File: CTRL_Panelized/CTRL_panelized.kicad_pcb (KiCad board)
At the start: 2 copper layers, 72.8 x 111.2 mm, 101 parts, among them J1 503480-0540, J1 5034801400, J2 503480-0440, J2 503480-0800, J2 AYF530365TA, J3 5034801400, J4 503480-0440, J5 503480-0540, U1 74LVC1G08, U1 DRV5033FAxDBZ, U2 74LVC1G08, U2 DRV5033FAxDBZ

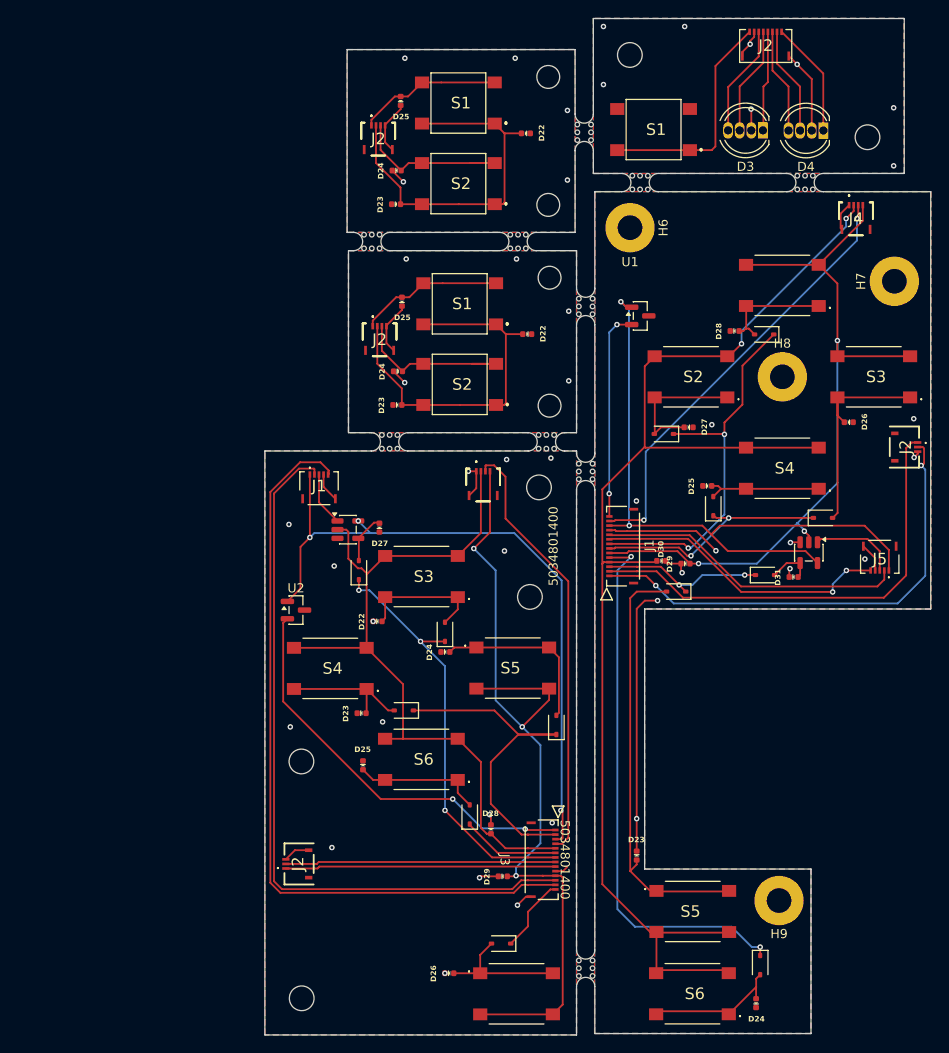
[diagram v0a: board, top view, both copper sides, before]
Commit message: Routed 1V8, 3V3 and 9V voltage regulators
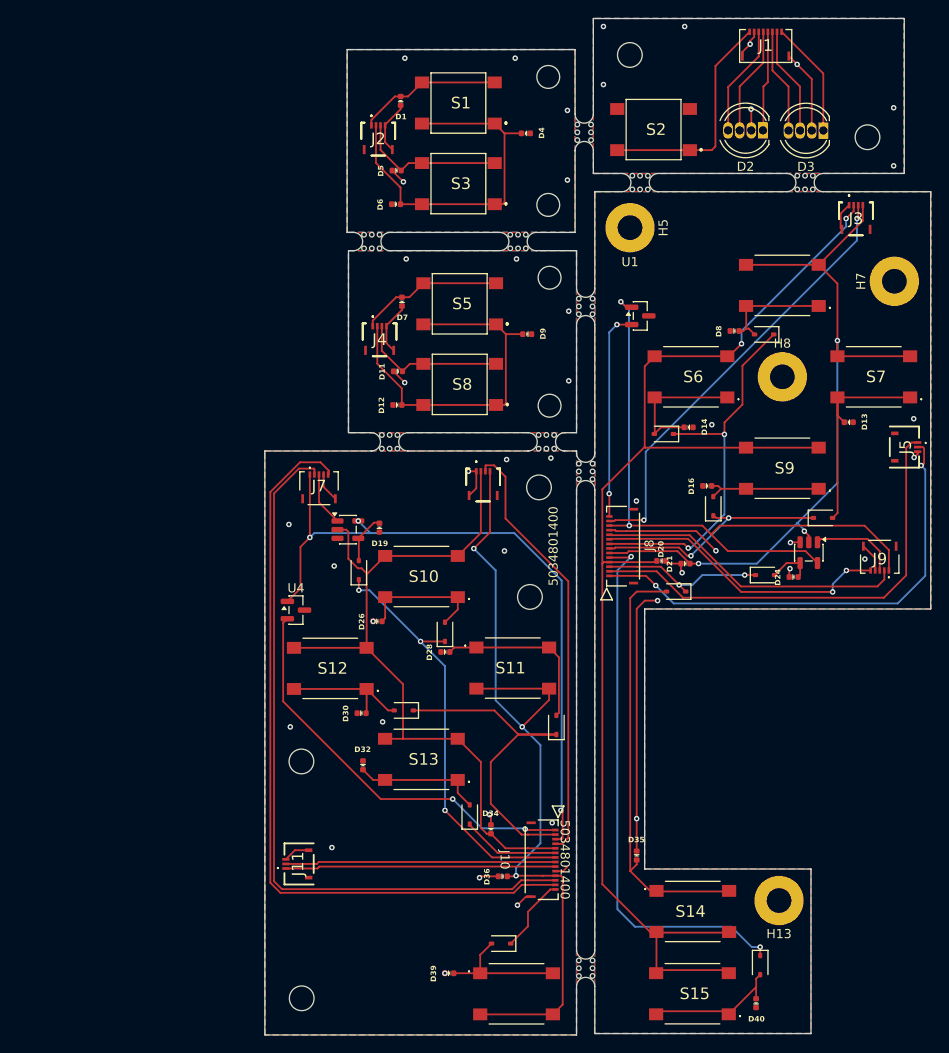
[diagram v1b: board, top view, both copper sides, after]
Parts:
- renumbered D25 to D1, D1 to D10, D24 to D11, D23 to D12, D26 to D13, D27 to D14, D2 to D15, D25 to D16, D4 to D17, D3 to D18, D27 to D19, D3 to D2, D30 to D20, D29 to D21, D8 to D22, D7 to D23, D31 to D24, D5 to D25, D22 to D26, D3 to D27, D24 to D28, D4 to D29, D4 to D3, D23 to D30, D5 to D31, D25 to D32, D6 to D33, D28 to D34, D23 to D35, D29 to D36, D7 to D37, D6 to D38, D26 to D39, D22 to D4, D24 to D40, D24 to D5, D23 to D6, D25 to D7, D28 to D8, D22 to D9, H1 to H10, H2 to H11, H3 to H12, H9 to H13, H4 to H14, H3 to H2, H2 to H3, H2 to H4, H6 to H5, H3 to H6, H2 to H9, J2 to J1, J3 to J10, J2 to J11, J4 to J3, J2 to J4, J2 to J5, J4 to J6, J1 to J7, J1 to J8, J5 to J9, S3 to S10, S5 to S11, S4 to S12, S6 to S13, S5 to S14, S6 to S15, S7 to S16, S1 to S2, S2 to S3, S1 to S4, S1 to S5, S2 to S6, S3 to S7, S2 to S8, S4 to S9, U1 to U2, U2 to U3, U2 to U4, kibuzzard-6A70E37C to kibuzzard-1, kibuzzard-6A70E37C to kibuzzard-2, kibuzzard-6A187131 to kibuzzard-3, kibuzzard-6A186FEC to kibuzzard-4, kibuzzard-6A19F3B7 to kibuzzard-5, kibuzzard-6A187131 to kibuzzard-6
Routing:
- net ColA: track 38.2 -> 32.9 mm
- net +3V3: track 149.7 -> 149.2 mm

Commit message: Some fixes and stuff. i guess.
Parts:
- removed the REF** at (120.7, 54.1)
- removed the REF** at (103.5, 54.1)
- added REF**: MouseBite-Slot_2.0x2.0mm_outset_D0.5mm_P0.85mm_3h, Panelization:MouseBite-Slot_2.0x2.0mm_outset_D0.5mm_P0.85mm_3h, F.Cu at (124.0, 40.2)
- moved D9 75.0 mm to (82.5, 109.0)
- moved J4 75.0 mm to (66.4, 109.7)
- moved D11 75.0 mm to (68.4, 113.1)
- moved D12 75.0 mm to (68.3, 116.8)
- moved D7 75.0 mm to (68.8, 105.5)
- moved H6 75.0 mm to (84.9, 102.9)
- moved H9 75.0 mm to (84.9, 116.9)
- moved REF** 75.0 mm to (89.9, 106.0)
- moved S5 75.0 mm to (75.1, 105.7)
- moved S8 75.0 mm to (75.1, 114.5)
- moved kibuzzard-2 75.0 mm to (72.7, 117.9)
- moved D1 74.9 mm to (68.8, 83.5)
- moved D4 74.9 mm to (82.5, 87.1)
- moved D5 74.9 mm to (68.4, 91.1)
- moved D6 74.9 mm to (68.3, 94.8)
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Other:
- board size 72.8 x 111.2 mm -> 99.8 x 92.2 mm

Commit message: Fixed 3DS Volume slider connector (3 -> 4pin)*
*Changed only in CTRL_Panelized. Seperated PCBs will be updated once all changes are done.
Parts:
- J11, J5: value AYF530365TA -> 503480-0440; footprint AYF530365TA:AYF530365T -> 503480-0440:5034800440
- moved J11 0.25 mm to (93.6, 101.5)
- moved J5 0.24 mm to (159.8, 55.4)
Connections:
- J11 pad 1: SL_VIN -> GND
- J11 pad 2: SL_VOL -> SL_VIN
- J11 pad 3: GND -> SL_VOL
- J5 pad 1: SL_VIN -> GND
- J5 pad 2: SL_BRI -> SL_VIN
- J5 pad 3: GND -> SL_BRI

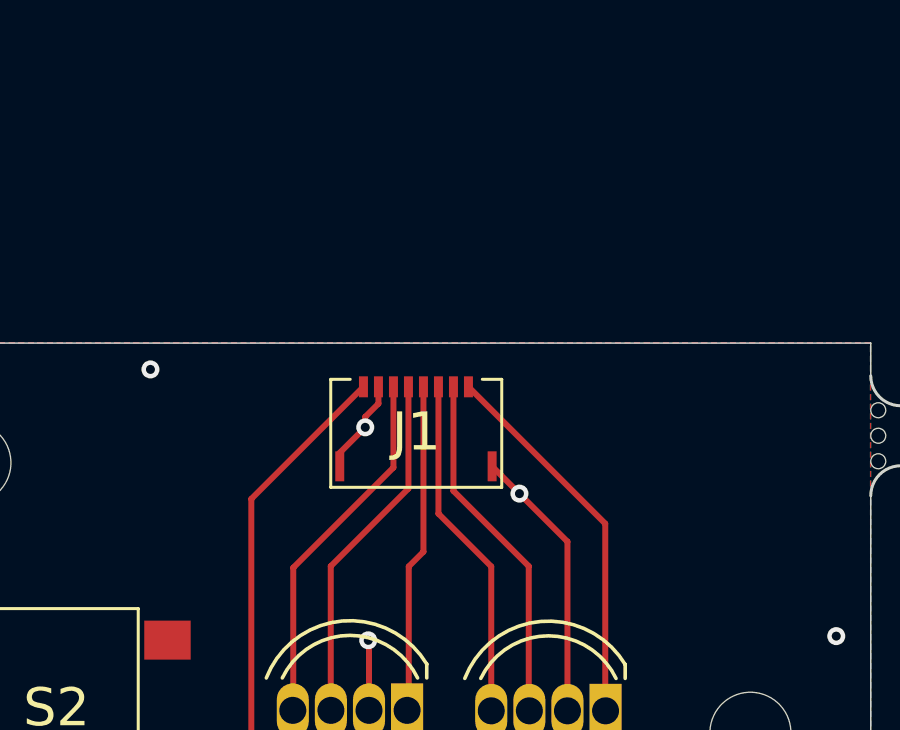
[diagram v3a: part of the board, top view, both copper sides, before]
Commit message: Majorly reworked Display system, condensed and fixed BOM, and many other schematic and design cleanups. \Programs folder was also cleaned up.
Everything is still a work in progress, many things are now unfinished, especially the PCB.
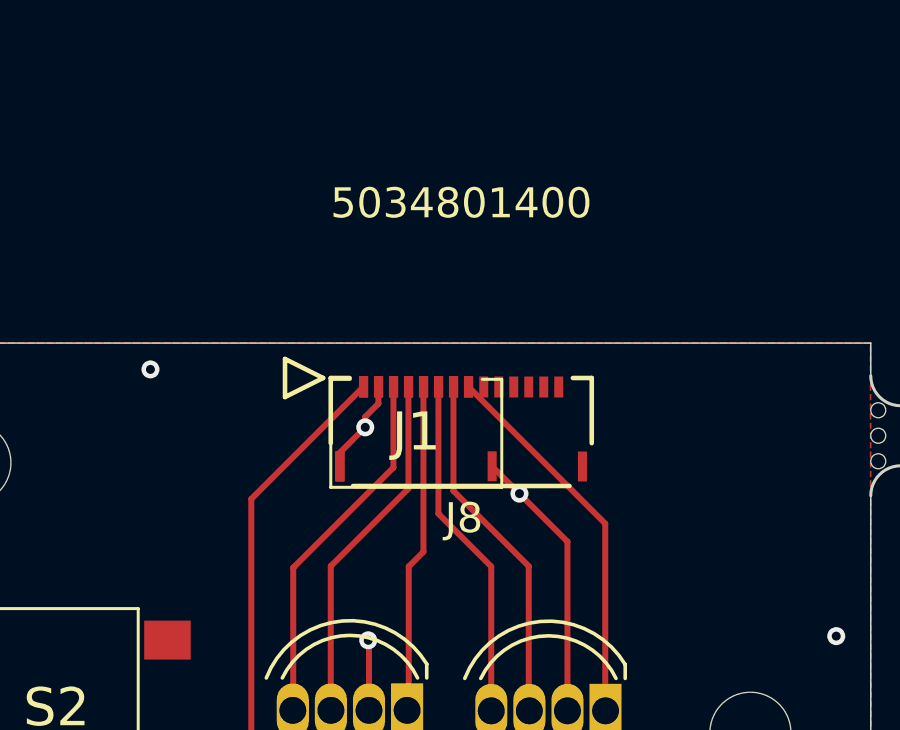
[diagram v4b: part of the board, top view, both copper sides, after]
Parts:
- added J8: 5034801400, 5034801400:5034801400, F.Cu at (110.3, 40.1)

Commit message: Repository push for Project Deadline :o
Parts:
- removed the J8 at (110.3, 40.1)
